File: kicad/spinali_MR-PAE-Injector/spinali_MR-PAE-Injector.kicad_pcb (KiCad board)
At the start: 6 copper layers, 36.5 x 46 mm, 35 parts, among them J1 5055780421, J13 5055780421, J3 CAN0A, J4 CAN0B, Q1 BUK6D56-60EX, U1 LM74700, U3 LM5160DNTJ

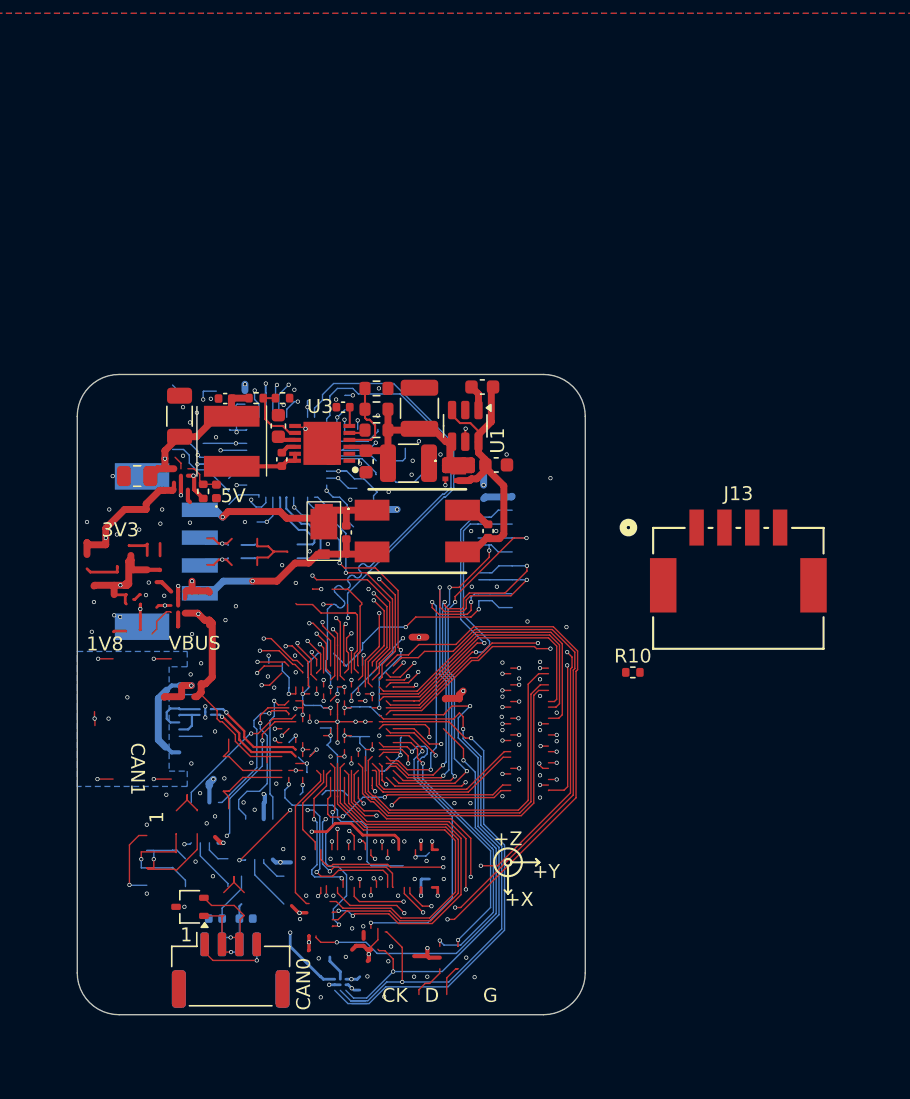
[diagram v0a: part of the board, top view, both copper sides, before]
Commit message: ongoing edits and prep
added symbols for 2 pin  and 3 pin headers.
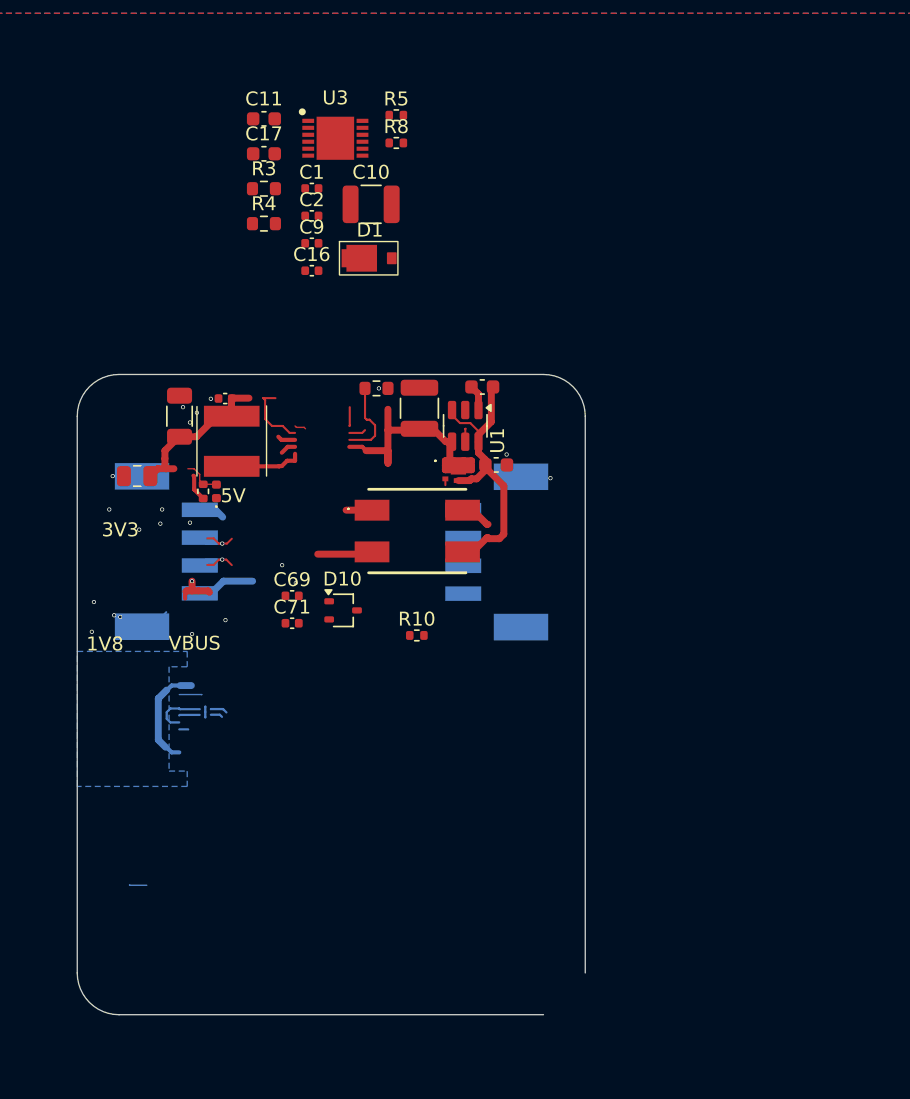
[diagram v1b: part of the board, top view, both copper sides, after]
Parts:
- removed J3: CAN0A, Connector_JST:JST_GH_SM04B-GHS-TB_1x04-1MP_P1.25mm_Horizontal
- removed J4: CAN0B, Connector_JST:JST_GH_SM04B-GHS-TB_1x04-1MP_P1.25mm_Horizontal
- C69, C71: moved to F.Cu
- J13: moved to B.Cu
- R3: value 100k 1% 75V -> 162k 1% 75V
- moved G*** 42.9 mm to (128.8, 67.2)
- moved C2 25.9 mm to (99.1, 64.6), turned to 0 degrees
- moved C11 25.7 mm to (95.6, 57.6), turned to 0 degrees
- moved C1 24.8 mm to (99.1, 62.6), turned to 0 degrees
- moved D10 24.0 mm to (101.3, 92.9), turned to 0 degrees
- moved C69 23.4 mm to (97.6, 91.9)
- moved R5 22.7 mm to (105.1, 57.3)
- moved U3 21.9 mm to (100.7, 59.0), turned to 0 degrees
- moved C71 21.9 mm to (97.6, 93.8)
- moved D1 20.6 mm to (103.7, 67.6), turned to 0 degrees
- moved R8 20.1 mm to (105.1, 59.3)
- moved C17 19.6 mm to (95.6, 60.1), turned to 0 degrees
- moved R3 19.1 mm to (95.6, 62.6), turned to 0 degrees
- moved C10 18.8 mm to (103.3, 63.7), turned to 0 degrees
- moved R10 15.7 mm to (106.6, 94.7)
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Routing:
- net (no net): track 2619.8 -> 984.5 mm, vias 233 -> 1
- net GND: track 32.7 -> 6.07 mm, vias 152 -> 21
- net Net-(D10-A2): track 13.4 -> 0.00 mm, vias 1 -> 0
- net Net-(C1-Pad2): track 15.6 -> 3.73 mm, vias 1 -> 0
- net Net-(D10-A1): track 8.87 -> 0.00 mm, vias 1 -> 0
- net Net-(C1-Pad1): track 14.7 -> 8.13 mm, vias 1 -> 0
- net Net-(J3-Pad1): track 5.70 -> 0.00 mm, vias 1 -> 0
- net Net-(C12-Pad1): track 18.1 -> 17.7 mm, vias 2 -> 0
- net Net-(Q1-G): vias 2 -> 0
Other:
- board text removed: "+X"
- board text removed: "+Y"
- board text removed: "+Z"
- board text removed: "CAN0"
- board text removed: "CAN1"
- board text removed: "CK"
- board text removed: "CLK"
- board text removed: "D"
- board text removed: "G"
- board text removed: "GND"

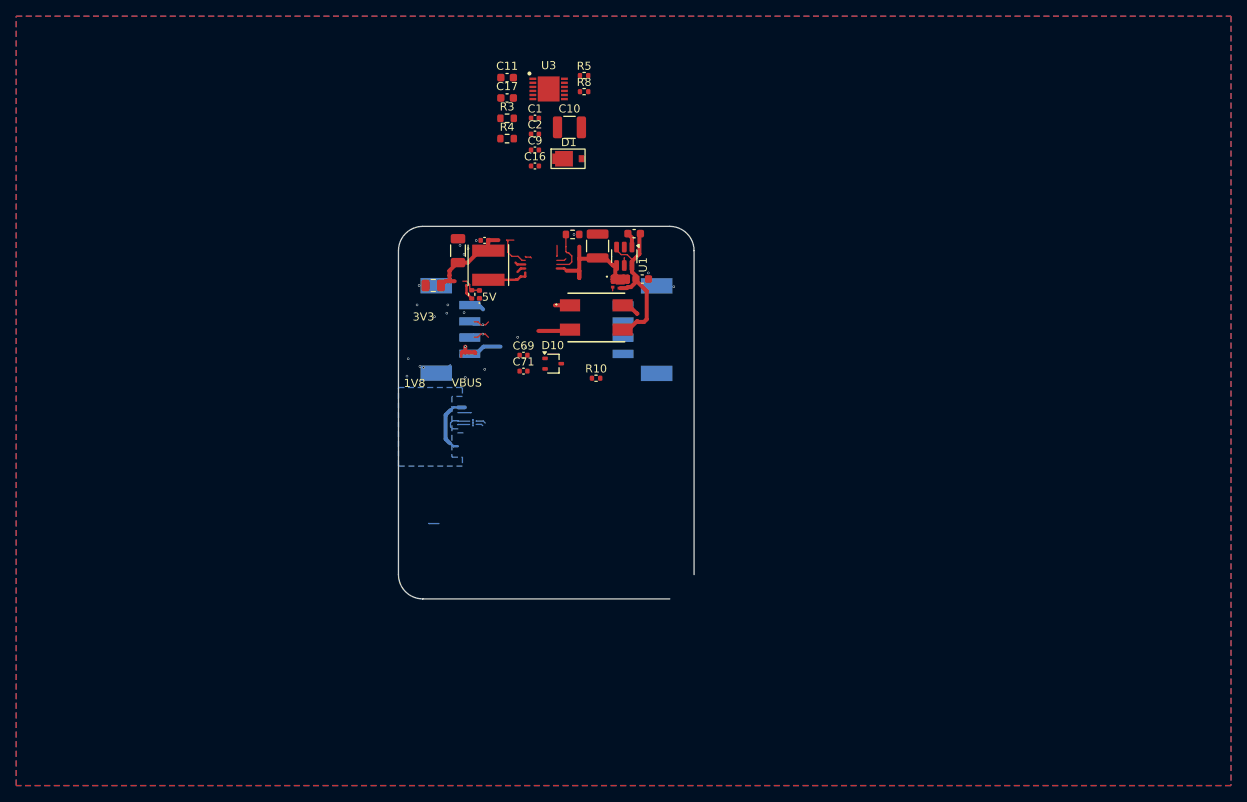
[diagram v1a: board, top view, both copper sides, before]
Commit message: removed reverse polarity
MAY put it back in for the screw terminal connection.
Testing rough board sizes
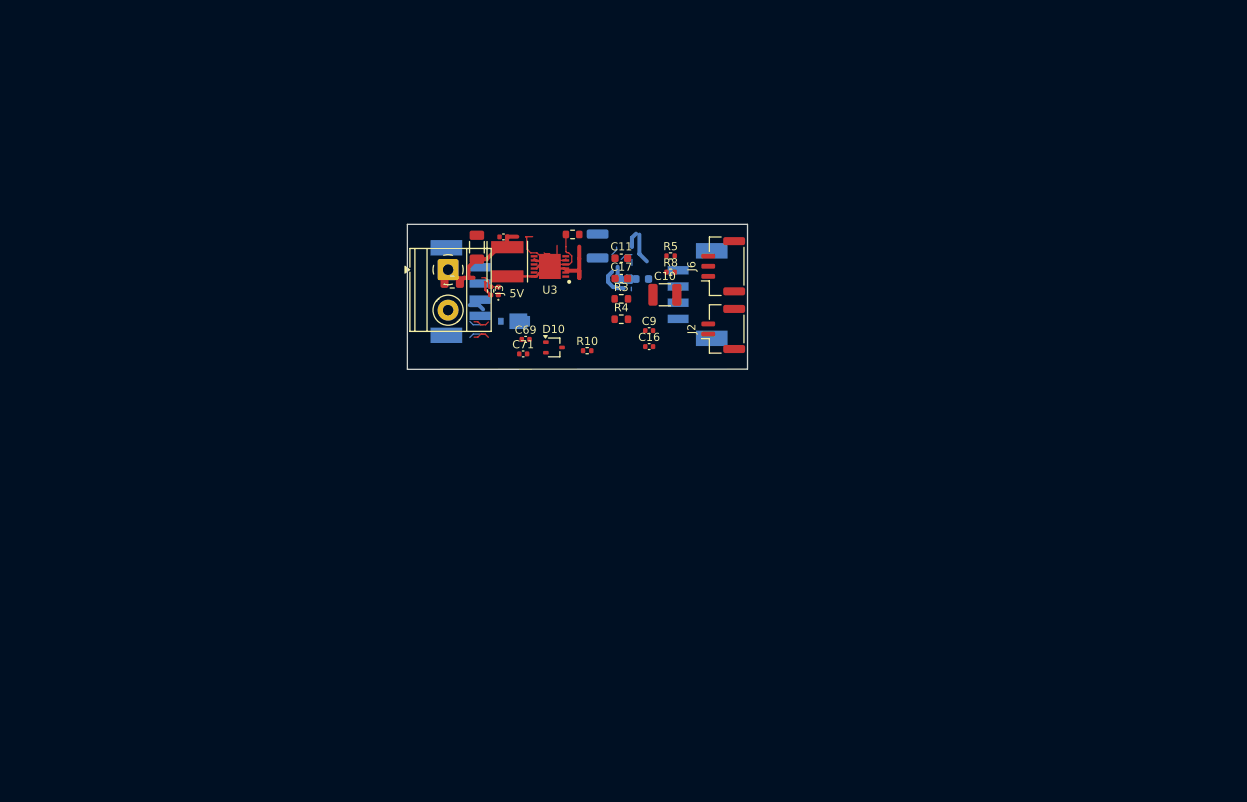
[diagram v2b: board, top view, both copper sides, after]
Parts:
- removed C1, C2: 1nF 100V, Capacitor_SMD:C_0402_1005Metric
- removed C5: 100nF 100V, Capacitor_SMD:C_0603_1608Metric
- removed L1: ACM7060-301-2PL-TL01, Inductors:ACM70603012PLTL01
- removed Q1: BUK6D56-60EX, MOSFETs:BUK6D5660EX
- removed U1: LM74700, Package_TO_SOT_SMD:SOT-23-6
- added J2: Conn_01x02_MountingPin, Connector_JST:JST_GH_SM02B-GHS-TB_1x02-1MP_P1.25mm_Horizontal, F.Cu at (122.3, 88.6)
- added J3: Screw_Terminal_01x02, TerminalBlock_Phoenix:TerminalBlock_Phoenix_MKDS-1,5-2_1x02_P5.00mm_Horizontal, F.Cu at (88.3, 81.3)
- added J6: Conn_01x03, Connector_JST:JST_GH_SM03B-GHS-TB_1x03-1MP_P1.25mm_Horizontal, F.Cu at (122.3, 80.9)
- C3: value 22nF 100V -> 1uF 100V; moved to B.Cu
- C4, D1: moved to B.Cu
- moved R4 26.4 mm to (109.7, 87.4)
- moved C11 26.4 mm to (109.7, 79.9)
- moved C17 26.4 mm to (109.7, 82.4)
- moved R3 26.4 mm to (109.7, 84.9)
- moved C16 26.4 mm to (113.2, 90.8)
- moved C9 26.4 mm to (113.2, 88.8)
- moved R8 24.7 mm to (115.8, 81.6)
- moved R5 24.7 mm to (115.8, 79.6)
- moved C10 23.8 mm to (115.1, 84.4)
- moved U3 21.9 mm to (100.9, 80.9), turned to 180 degrees
- moved D1 21.5 mm to (95.9, 87.7), turned to 180 degrees
- moved J13 8.06 mm to (121.1, 84.4)
- moved J1 4.84 mm to (87.9, 84.0)
- moved R10 3.57 mm to (105.5, 91.3)
- moved C12 2.37 mm to (95.2, 77.3)
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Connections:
- C12 pad 1: Net-(C12-Pad1) -> +5V
- C13 pad 2: Net-(C12-Pad1) -> +5V
- C14 pad 2: Net-(C12-Pad1) -> +5V
- C3 pad 2: Net-(Q1-S) -> +BATT
- C69 pad 1: Net-(D10-A1) -> +5V
- D1 pad 1: Net-(C1-Pad2) -> GND
- D1 pad 2: Net-(C1-Pad1) -> +BATT
- D10 pad 1: Net-(D10-A1) -> +5V
- J1 pad 1: Net-(C1-Pad1) -> +BATT
- J1 pad 4: Net-(C1-Pad2) -> GND
- J13 pad 1: Net-(C1-Pad1) -> +BATT
- J13 pad 4: Net-(C1-Pad1) -> GND
- L2 pad 2: Net-(C12-Pad1) -> +5V
- R5 pad 1: Net-(C12-Pad1) -> +5V
- R6 pad 1: Net-(C12-Pad1) -> +5V
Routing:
- net (no net): track 984.5 -> 16.2 mm, vias 1 -> 0
- net Net-(Q1-S): track 21.5 -> 0.00 mm
- net Net-(C12-Pad1): track 17.7 -> 0.00 mm
- net +5V: track 0.00 -> 15.1 mm
- net +BATT: track 22.2 -> 8.42 mm
- net Net-(C1-Pad1): track 8.13 -> 0.00 mm
- net Net-(Q1-G): track 6.06 -> 0.00 mm
- net Net-(C1-Pad2): track 3.73 -> 0.00 mm
- net GND: track 6.07 -> 9.44 mm, vias 21 -> 0
- net Net-(U1-VCAP): track 1.87 -> 0.00 mm
- net ENET0_TRX_N: track 3.86 -> 2.07 mm, vias 1 -> 0
- net ENET0_TRX_P: track 3.88 -> 3.95 mm, vias 1 -> 0
- removed copper zone on B.Cu, net (none)
- removed copper zone on In2.Cu, net (none)
- removed copper zone on B.Cu, net GND
- removed copper zone on F.Cu, net GND
- removed copper zone on In1.Cu, net GND
- removed copper zone on In3.Cu, net GND
- removed copper zone on In4.Cu, net GND
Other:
- board size 36.5 x 46 mm -> 42 x 17.9 mm
- copper layers 6 -> 4
- board text removed: "1V8"
- board text removed: "3V3"
- board text removed: "VBUS"
